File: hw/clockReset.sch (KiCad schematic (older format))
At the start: 6 parts

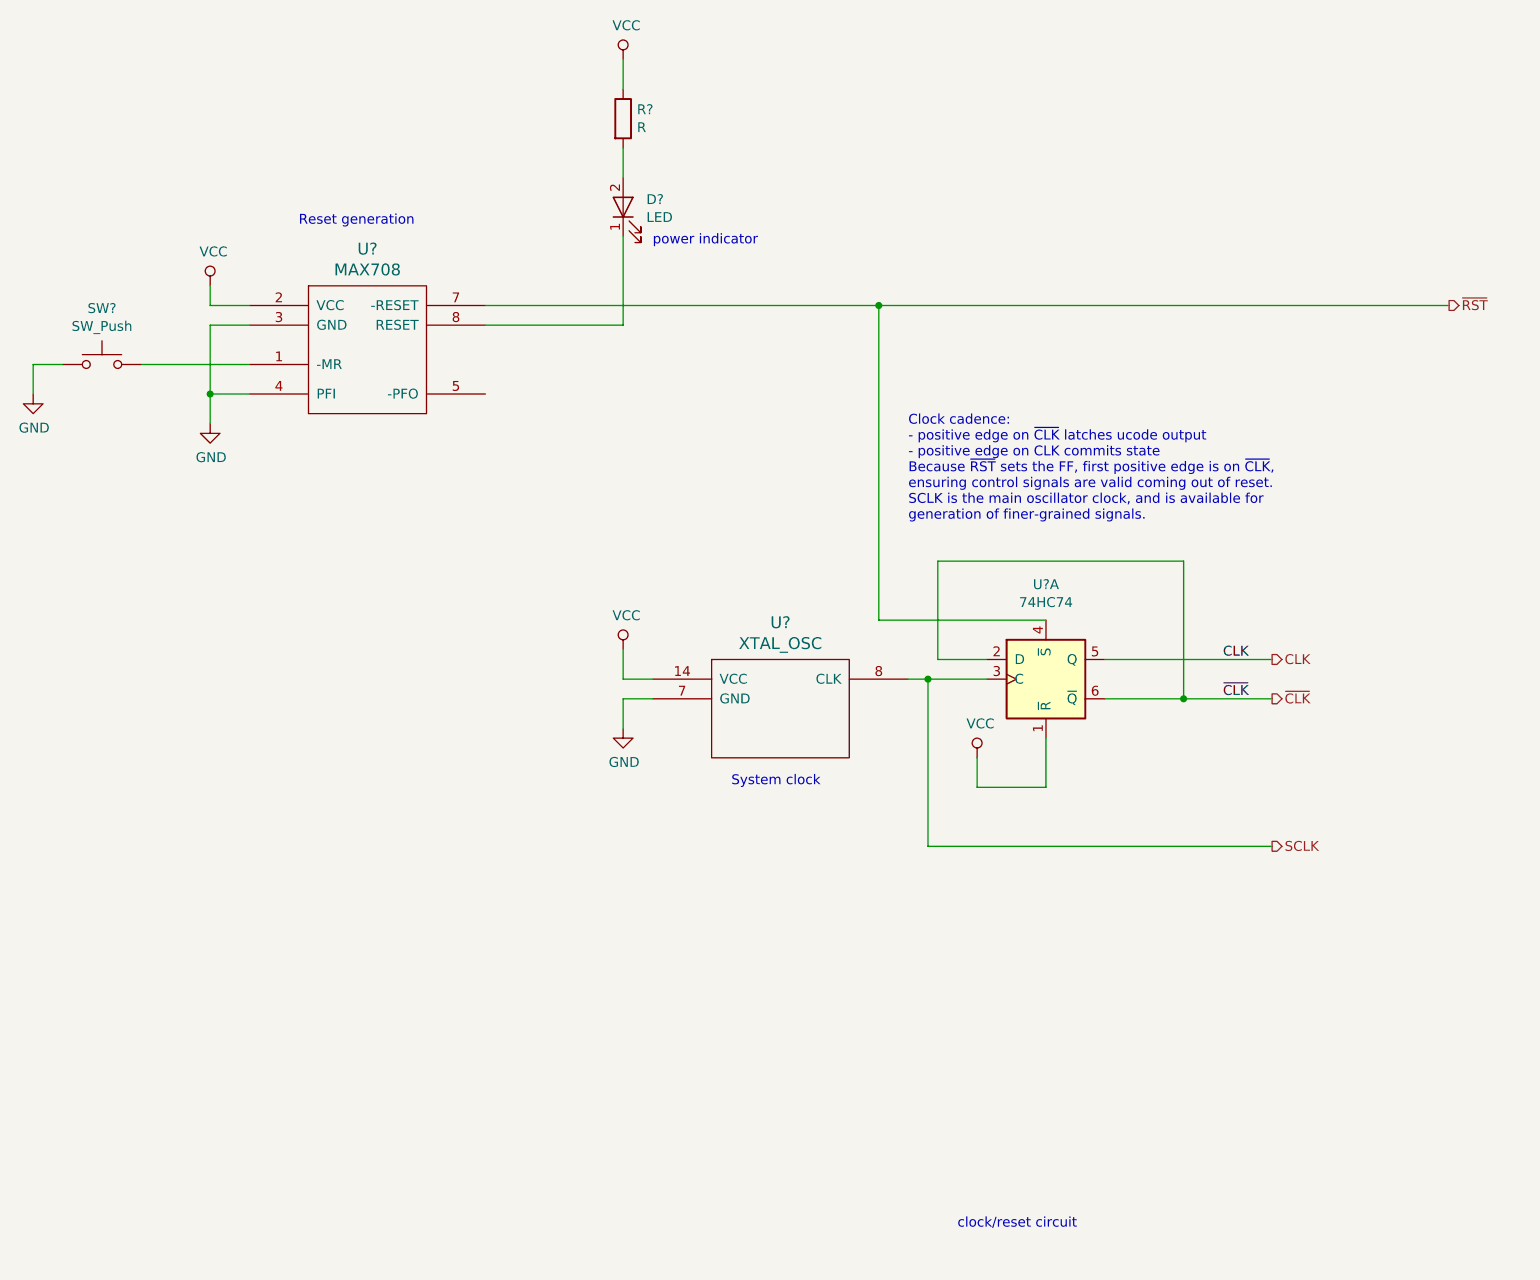
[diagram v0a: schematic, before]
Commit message: some schematic cleanups and descriptive text added
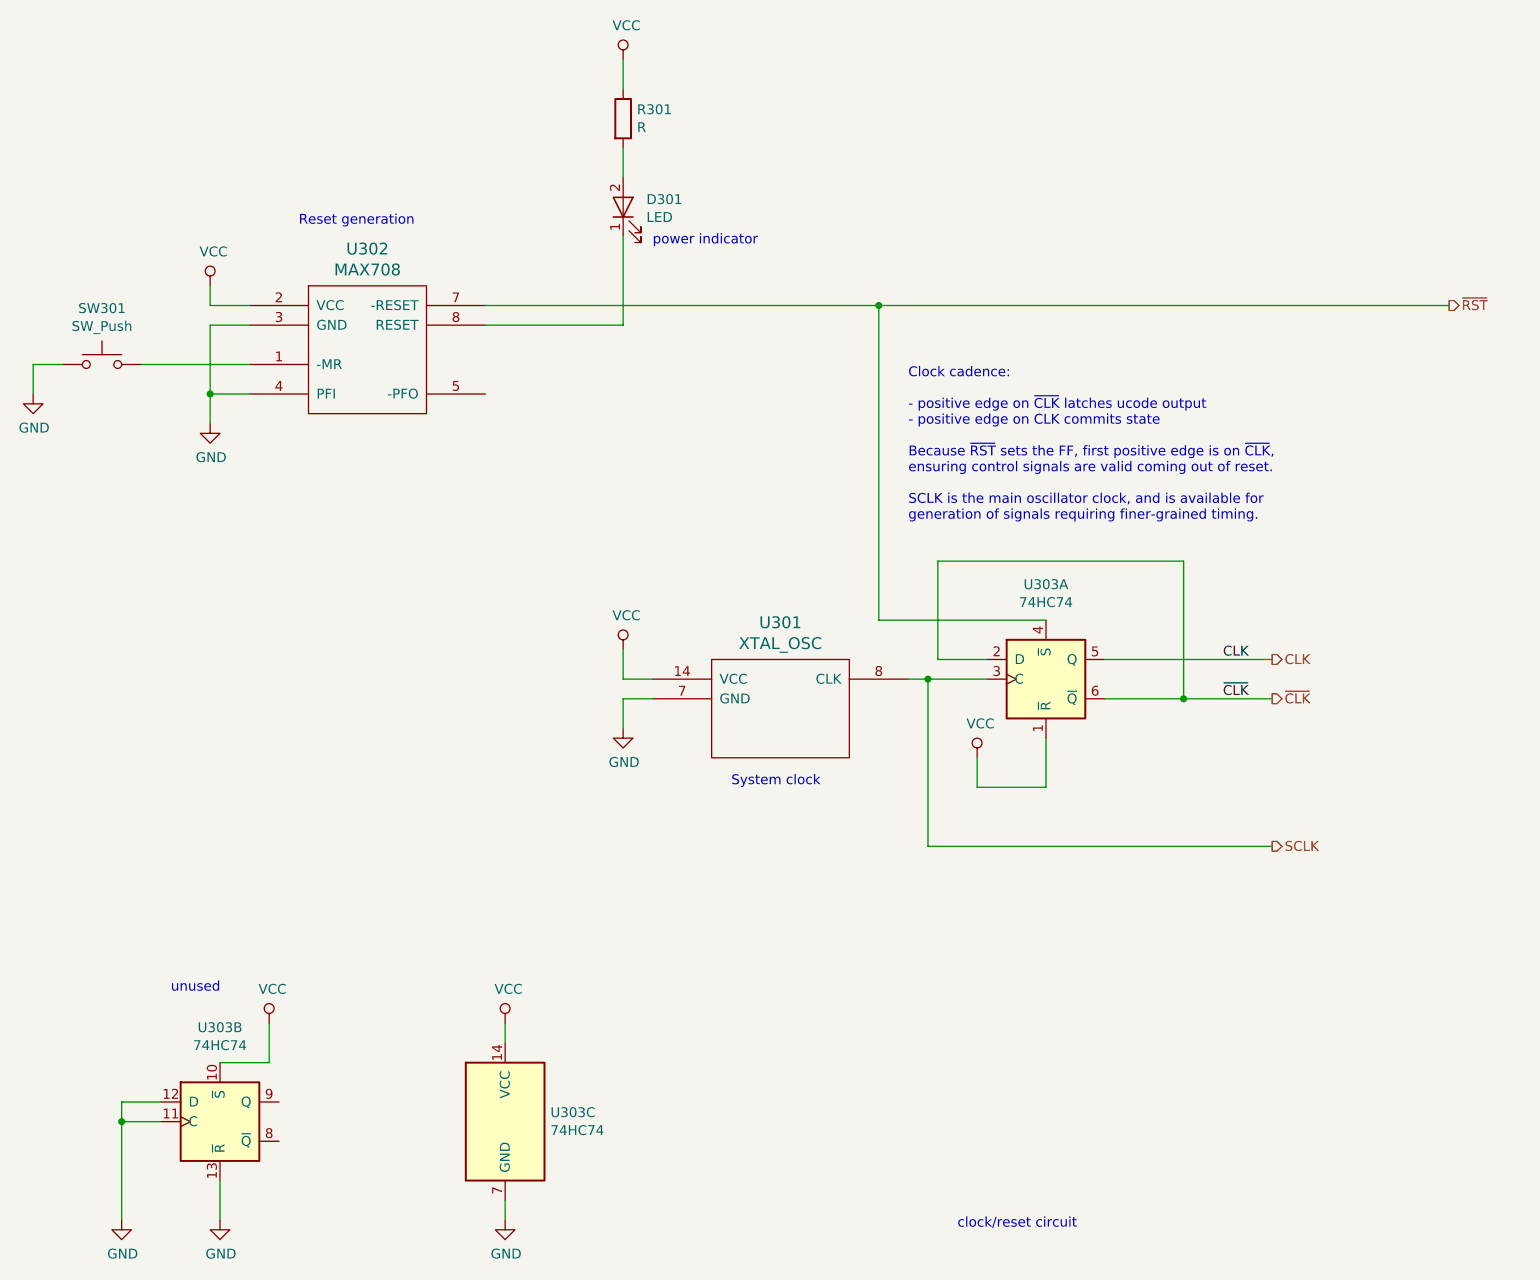
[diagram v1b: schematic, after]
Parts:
- added unit 2 of U303
- added unit 3 of U303
- gave numbers to parts that had none: 6
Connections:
- net GND: now also U303.11 (C), U303.12 (D), U303.13 (~R), U303.7 (GND)
- net VCC: now also U303.10 (~S), U303.14 (VCC)
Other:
- note added: "Clock cadence:\n\n- positive edge on ~CLK~ latches ucode output\n- positive edge on CLK commits state\n\nBecause ~RST~ sets the FF, first positive edge is on ~CLK~,\nensuring control signals are valid coming out of reset.\n\nSCLK is the main oscillator clock, and is available for\ngeneration of signals requiring finer-grained timing."
- note added: "unused"
- note removed: "Clock cadence:\n- positive edge on ~CLK~ latches ucode output\n- positive edge on CLK commits state\nBecause ~RST~ sets the FF, first positive edge is on ~CLK~,\nensuring control signals are valid coming out of reset.\nSCLK is the main oscillator clock, and is available for\ngeneration of finer-grained signals."
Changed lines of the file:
@@
 $Descr USLetter 11000 8500
 encoding utf-8
-Sheet 5 4
+Sheet 4 4
 Title ""
 Date ""
@@
 P 5450 4300
 AR Path="/5DA2EB51/5DABBACF" Ref="U?"  Part="1"
-AR Path="/5DAB38C5/5DABBACF" Ref="U?"  Part="1"
-F 0 "U?" H 5450 4737 60  0000 C CNN
+AR Path="/5DAB38C5/5DABBACF" Ref="U301"  Part="1"
+F 0 "U301" H 5450 4737 60  0000 C CNN
 F 1 "XTAL_OSC" H 5450 4631 60  0000 C CNN
 F 2 "" H 5450 4300 60  0000 C CNN
@@
 P 6800 4150
 AR Path="/5DA2EB51/5DABBAD5" Ref="U?"  Part="1"
-AR Path="/5DAB38C5/5DABBAD5" Ref="U?"  Part="1"
-F 0 "U?" H 6800 4631 50  0000 C CNN
+AR Path="/5DAB38C5/5DABBAD5" Ref="U303"  Part="1"
+F 0 "U303" H 6800 4631 50  0000 C CNN
 F 1 "74HC74" H 6800 4540 50  0000 C CNN
 F 2 "" H 6800 4150 50  0001 C CNN
@@
 	6250 4050 6500 4050
 Text Notes 6100 3350 0    50   ~ 0
-Clock cadence:\n- positive edge on ~CLK~ latches ucode output\n- positive edge on CLK commits state\nBecause ~RST~ sets the FF, first positive edge is on ~CLK~,\nensuring control signals are valid coming out of reset.\nSCLK is the main oscillator clock, and is available for\ngeneration of finer-grained signals.
+Clock cadence:\n\n- positive edge on ~CLK~ latches ucode output\n- positive edge on CLK commits state\n\nBecause ~RST~ sets the FF, first positive edge is on ~CLK~,\nensuring control signals are valid coming out of reset.\n\nSCLK is the main oscillator clock, and is available for\ngeneration of signals requiring finer-grained timing.
 Wire Wire Line
 	6800 3850 5950 3850
@@
 P 3350 2450
 AR Path="/5DACE71F/5DABDA79" Ref="U?"  Part="1"
-AR Path="/5DAB38C5/5DABDA79" Ref="U?"  Part="1"
-F 0 "U?" H 3350 2937 60  0000 C CNN
+AR Path="/5DAB38C5/5DABDA79" Ref="U302"  Part="1"
+F 0 "U302" H 3350 2937 60  0000 C CNN
 F 1 "MAX708" H 3350 2831 60  0000 C CNN
 F 2 "" H 3350 2450 60  0000 C CNN
@@
 P 2000 2550
 AR Path="/5DACE71F/5DABDA7F" Ref="SW?"  Part="1"
-AR Path="/5DAB38C5/5DABDA7F" Ref="SW?"  Part="1"
-F 0 "SW?" H 2000 2835 50  0000 C CNN
+AR Path="/5DAB38C5/5DABDA7F" Ref="SW301"  Part="1"
+F 0 "SW301" H 2000 2835 50  0000 C CNN
 F 1 "SW_Push" H 2000 2744 50  0000 C CNN
 F 2 "" H 2000 2750 50  0001 C CNN
@@
 P 4650 1750
 AR Path="/5DACE71F/5DABDAA1" Ref="D?"  Part="1"
-AR Path="/5DAB38C5/5DABDAA1" Ref="D?"  Part="1"
-F 0 "D?" V 4689 1632 50  0000 R CNN
+AR Path="/5DAB38C5/5DABDAA1" Ref="D301"  Part="1"
+F 0 "D301" V 4689 1632 50  0000 R CNN
 F 1 "LED" V 4598 1632 50  0000 R CNN
 F 2 "" H 4650 1750 50  0001 C CNN
@@
 P 4650 1300
 AR Path="/5DACE71F/5DABDAA9" Ref="R?"  Part="1"
-AR Path="/5DAB38C5/5DABDAA9" Ref="R?"  Part="1"
-F 0 "R?" H 4720 1346 50  0000 L CNN
+AR Path="/5DAB38C5/5DABDAA9" Ref="R301"  Part="1"
+F 0 "R301" H 4720 1346 50  0000 L CNN
 F 1 "R" H 4720 1255 50  0000 L CNN
 F 2 "" V 4580 1300 50  0001 C CNN
@@
 Text Notes 6350 6950 0    50   ~ 0
 clock/reset circuit
+$Comp
+L 74xx:74HC74 U303
+U 2 1 5DADC92D
+P 2600 6400
+F 0 "U303" H 2600 6878 50  0000 C CNN
+F 1 "74HC74" H 2600 6787 50  0000 C CNN
+F 2 "" H 2600 6400 50  0001 C CNN
+F 3 "" H 2600 6400 50  0001 C CNN
+	2    2600 6400
+	1    0    0    -1
+$EndComp
+$Comp
+L 74xx:74HC74 U303
+U 3 1 5DADC9F1
+P 4050 6400
+F 0 "U303" H 4280 6446 50  0000 L CNN
+F 1 "74HC74" H 4280 6355 50  0000 L CNN
+F 2 "" H 4050 6400 50  0001 C CNN
+F 3 "" H 4050 6400 50  0001 C CNN
+	3    4050 6400
+	1    0    0    -1
+$EndComp
+Wire Wire Line
+	2600 6700 2600 6900
+$Comp
+L power:GND #PWR?
+U 1 1 5DADD0F1
+P 2600 6900
+F 0 "#PWR?" H 2600 6650 50  0001 C CNN
+F 1 "GND" H 2605 6727 50  0000 C CNN
+F 2 "" H 2600 6900 50  0001 C CNN
+F 3 "" H 2600 6900 50  0001 C CNN
+	1    2600 6900
+	1    0    0    -1
+$EndComp
+Wire Wire Line
+	2300 6400 2100 6400
+Wire Wire Line
+	2100 6400 2100 6900
+Wire Wire Line
+	2300 6300 2100 6300
+Wire Wire Line
+	2100 6300 2100 6400
+Connection ~ 2100 6400
+$Comp
+L power:GND #PWR?
+U 1 1 5DADDF7C
+P 2100 6900
+F 0 "#PWR?" H 2100 6650 50  0001 C CNN
+F 1 "GND" H 2105 6727 50  0000 C CNN
+F 2 "" H 2100 6900 50  0001 C CNN
+F 3 "" H 2100 6900 50  0001 C CNN
+	1    2100 6900
+	1    0    0    -1
+$EndComp
+Wire Wire Line
+	2600 6100 2850 6100
+Wire Wire Line
+	2850 6100 2850 5900
+$Comp
+L power:VCC #PWR?
+U 1 1 5DADE844
+P 2850 5900
+F 0 "#PWR?" H 2850 5750 50  0001 C CNN
+F 1 "VCC" H 2867 6073 50  0000 C CNN
+F 2 "" H 2850 5900 50  0001 C CNN
+F 3 "" H 2850 5900 50  0001 C CNN
+	1    2850 5900
+	1    0    0    -1
+$EndComp
+Wire Wire Line
+	4050 6000 4050 5900
+$Comp
+L power:VCC #PWR?
+U 1 1 5DAE0A62
+P 4050 5900
+F 0 "#PWR?" H 4050 5750 50  0001 C CNN
+F 1 "VCC" H 4067 6073 50  0000 C CNN
+F 2 "" H 4050 5900 50  0001 C CNN
+F 3 "" H 4050 5900 50  0001 C CNN
+	1    4050 5900
+	1    0    0    -1
+$EndComp
+Wire Wire Line
+	4050 6800 4050 6900
+$Comp
+L power:GND #PWR?
+U 1 1 5DAE1C0A
+P 4050 6900
+F 0 "#PWR?" H 4050 6650 50  0001 C CNN
+F 1 "GND" H 4055 6727 50  0000 C CNN
+F 2 "" H 4050 6900 50  0001 C CNN
+F 3 "" H 4050 6900 50  0001 C CNN
+	1    4050 6900
+	1    0    0    -1
+$EndComp
+Text Notes 2350 5750 0    50   ~ 0
+unused
 $EndSCHEMATC
